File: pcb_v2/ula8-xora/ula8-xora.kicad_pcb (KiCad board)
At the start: 2 copper layers, 54.4 x 61 mm, 11 parts, among them J1 ula8a, U1 74LS86, U2 74LS86, U3 74LS244

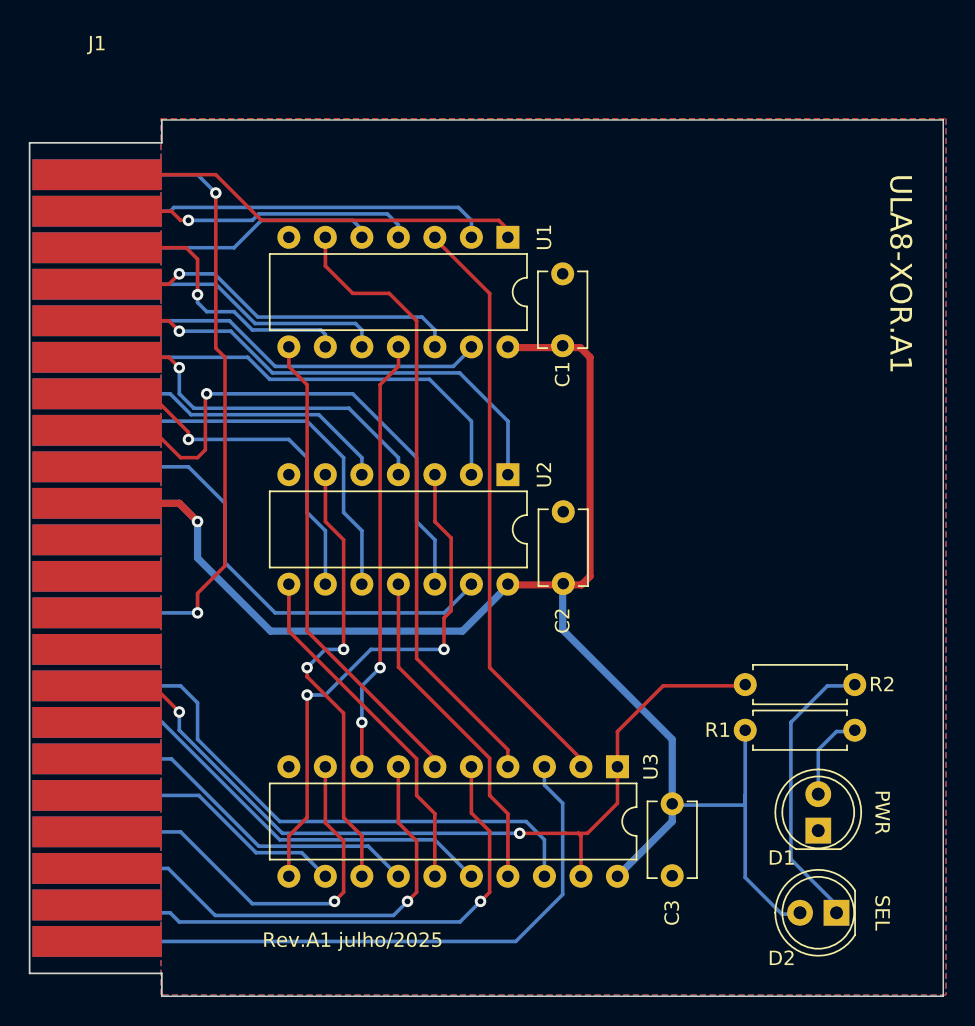
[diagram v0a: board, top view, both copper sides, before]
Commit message: revisao completa; mgrfa agora inclui sr8 e sgrda; remover estes dois no proximo commit
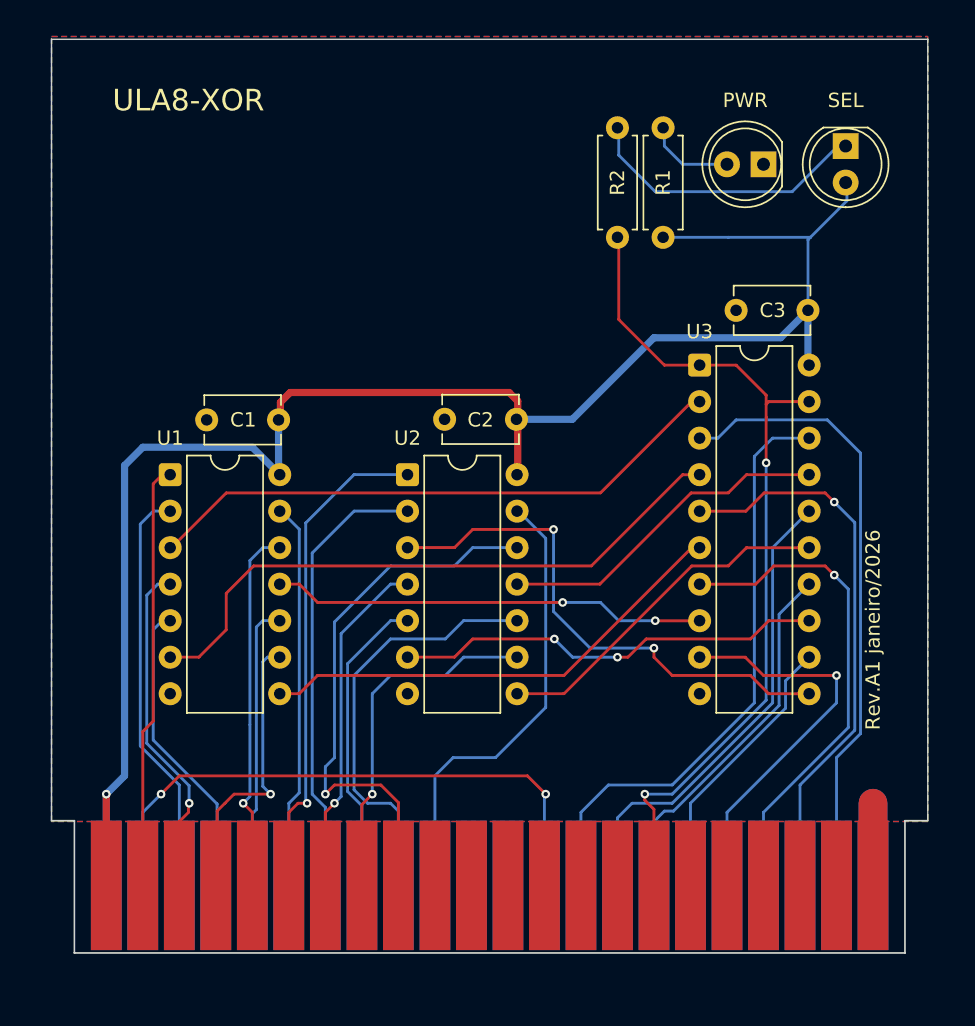
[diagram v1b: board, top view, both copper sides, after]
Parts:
- moved D2 53.3 mm to (93.3, 30.5), turned to -90 degrees
- moved J1 49.4 mm to (41.9, 81.9), turned to 90 degrees
- moved D1 46.5 mm to (87.6, 31.8), turned to 180 degrees
- moved R2 42.1 mm to (77.5, 29.2), turned to -90 degrees
- moved C3 39.6 mm to (85.7, 41.9), turned to 0 degrees
- moved R1 34.8 mm to (80.6, 36.8), turned to 90 degrees
- moved U1 28.7 mm to (46.4, 53.3), turned to 0 degrees
- moved U3 28.5 mm to (83.2, 45.7), turned to 0 degrees
- moved C1 26.8 mm to (48.9, 49.5), turned to 0 degrees
- moved C2 10.5 mm to (65.4, 49.5), turned to 0 degrees
- moved U2 6.98 mm to (62.9, 53.3), turned to 0 degrees
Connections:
- J1 pad 1: lower_bus0 -> +5V
- J1 pad 10: +5V -> unconnected-(J1-Pin_10-Pad10)
- J1 pad 11: GND -> unconnected-(J1-Pin_11-Pad11)
- J1 pad 15: n_select -> unconnected-(J1-Pin_15-Pad15)
- J1 pad 16: unconnected-(J1-Pad16) -> ~{select}
- J1 pad 2: lower_bus1 -> lower_bus0
- J1 pad 22: unconnected-(J1-Pad22) -> GND
- J1 pad 23: /carry -> +5V
- J1 pad 24: upper_bus0 -> carry
- J1 pad 25: upper_bus1 -> upper_bus0
- J1 pad 26: upper_bus2 -> upper_bus1
- J1 pad 27: upper_bus3 -> upper_bus2
- J1 pad 28: upper_bus4 -> upper_bus3
- J1 pad 29: upper_bus5 -> upper_bus4
- J1 pad 3: lower_bus2 -> lower_bus1
- J1 pad 30: upper_bus6 -> upper_bus5
- J1 pad 31: upper_bus7 -> upper_bus6
- J1 pad 32: +5V -> upper_bus7
- J1 pad 33: GND -> unconnected-(J1-Pin_33-Pad33)
- J1 pad 35: /carry -> carry
- J1 pad 36: unconnected-(J1-Pad36) -> ula_bus0
- J1 pad 37: ula_bus0 -> ula_bus1
- J1 pad 38: ula_bus1 -> ula_bus2
- J1 pad 39: ula_bus2 -> ula_bus3
- J1 pad 4: lower_bus3 -> lower_bus2
- J1 pad 40: ula_bus3 -> ula_bus4
- J1 pad 41: ula_bus4 -> ula_bus5
- J1 pad 42: ula_bus5 -> ula_bus6
- J1 pad 43: ula_bus6 -> ula_bus7
- J1 pad 44: ula_bus7 -> GND
- J1 pad 5: lower_bus4 -> lower_bus3
- J1 pad 6: lower_bus5 -> lower_bus4
- J1 pad 7: lower_bus6 -> lower_bus5
- J1 pad 8: lower_bus7 -> lower_bus6
- J1 pad 9: unconnected-(J1-Pad9) -> lower_bus7
- R2 pad 2: n_select -> ~{select}
- U3 pad 1: n_select -> ~{select}
- U3 pad 19: n_select -> ~{select}
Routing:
- net ~{select}: track 0.00 -> 60.2 mm, vias 0 -> 2
- net n_select: track 60.1 -> 0.00 mm, vias 2 -> 0
- net /carry: track 45.8 -> 0.00 mm, vias 2 -> 0
- net carry: track 0.00 -> 41.0 mm, vias 0 -> 2
- net GND: track 0.00 -> 11.4 mm
- net +5V: track 115.0 -> 122.8 mm
- net ula_bus1: track 30.3 -> 33.2 mm
- net ula_bus0: track 39.4 -> 41.7 mm
- net upper_bus6: track 27.9 -> 29.8 mm
- net lower_bus5: track 26.0 -> 24.1 mm
- net Net-(U3-I1b): track 31.7 -> 29.9 mm
- net upper_bus7: track 33.5 -> 31.7 mm
- net ula_bus2: track 24.1 -> 25.8 mm
- net ula_bus3: track 18.0 -> 19.3 mm
- net ula_bus6: track 37.7 -> 39.0 mm
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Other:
- board size 54.4 x 61 mm -> 61 x 54.4 mm
- board text added: "Rev.A1 janeiro/2026"
- board text added: "ULA8-XOR"
- board text removed: "Rev.A1 julho/2025"
- board text removed: "ULA8-XOR.A1"

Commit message: carry out depende de select
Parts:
- added C4: 100nF, Capacitor_THT:C_Disc_D5.1mm_W3.2mm_P5.00mm, F.Cu at (46.4, 41.2)
- added U4: 74LS125, Package_DIP:DIP-14_W7.62mm, F.Cu at (50.2, 43.8)
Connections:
- J1 pad 24: carry -> carry_in
- J1 pad 35: carry -> carry_out
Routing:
- net carry_out: track 0.00 -> 54.7 mm, vias 0 -> 1
- net carry_in: track 0.00 -> 44.3 mm, vias 0 -> 1
- net +5V: track 122.8 -> 167.0 mm
- net carry: track 41.0 -> 0.00 mm, vias 2 -> 0
- net ~{select}: track 60.2 -> 88.6 mm
- net GND: vias 0 -> 1
